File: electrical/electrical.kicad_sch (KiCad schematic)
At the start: 0 parts

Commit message: Added rotax
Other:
- sheet Rotax ports: added AIRCRAFT_AMPS_HI, AIRCRAFT_AMPS_LO, AIRCRAFT_GROUND, AIRCRAFT_POWER, ROTAX_CAN_GND, ROTAX_CAN_HI, ROTAX_CAN_LO; removed none
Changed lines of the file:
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@@
     (company "N915SN Angry Bird")
   )
-  (sheet (at 26.67 22.86) (size 20.32 25.4) (fields_autoplaced)
+  (sheet (at 19.05 19.05) (size 20.32 20.32) (fields_autoplaced)
     (stroke (width 0.1524) (type solid))
     (fill (color 0 0 0 0.0000))
-    (property "Sheetname" "Rotax" (at 26.67 22.1484 0)
+    (property "Sheetname" "Rotax" (at 19.05 18.3384 0)
       (effects (font (size 1.27 1.27)) (justify left bottom))
     )
-    (property "Sheetfile" "rotax.kicad_sch" (at 26.67 48.8446 0)
+    (property "Sheetfile" "rotax.kicad_sch" (at 19.05 39.9546 0)
       (effects (font (size 1.27 1.27)) (justify left top))
     )
+    (pin "AIRCRAFT_POWER" output (at 39.37 20.32 0)
+      (effects (font (size 1.27 1.27)) (justify right))
+    )
+    (pin "AIRCRAFT_GROUND" passive (at 39.37 22.86 0)
+      (effects (font (size 1.27 1.27)) (justify right))
+    )
+    (pin "AIRCRAFT_AMPS_HI" output (at 39.37 26.67 0)
+      (effects (font (size 1.27 1.27)) (justify right))
+    )
+    (pin "AIRCRAFT_AMPS_LO" output (at 39.37 29.21 0)
+      (effects (font (size 1.27 1.27)) (justify right))
+    )
+    (pin "ROTAX_CAN_LO" bidirectional (at 39.37 35.56 0)
+      (effects (font (size 1.27 1.27)) (justify right))
+    )
+    (pin "ROTAX_CAN_GND" passive (at 39.37 38.1 0)
+      (effects (font (size 1.27 1.27)) (justify right))
+    )
+    (pin "ROTAX_CAN_HI" bidirectional (at 39.37 33.02 0)
+      (effects (font (size 1.27 1.27)) (justify right))
+    )
     (instances

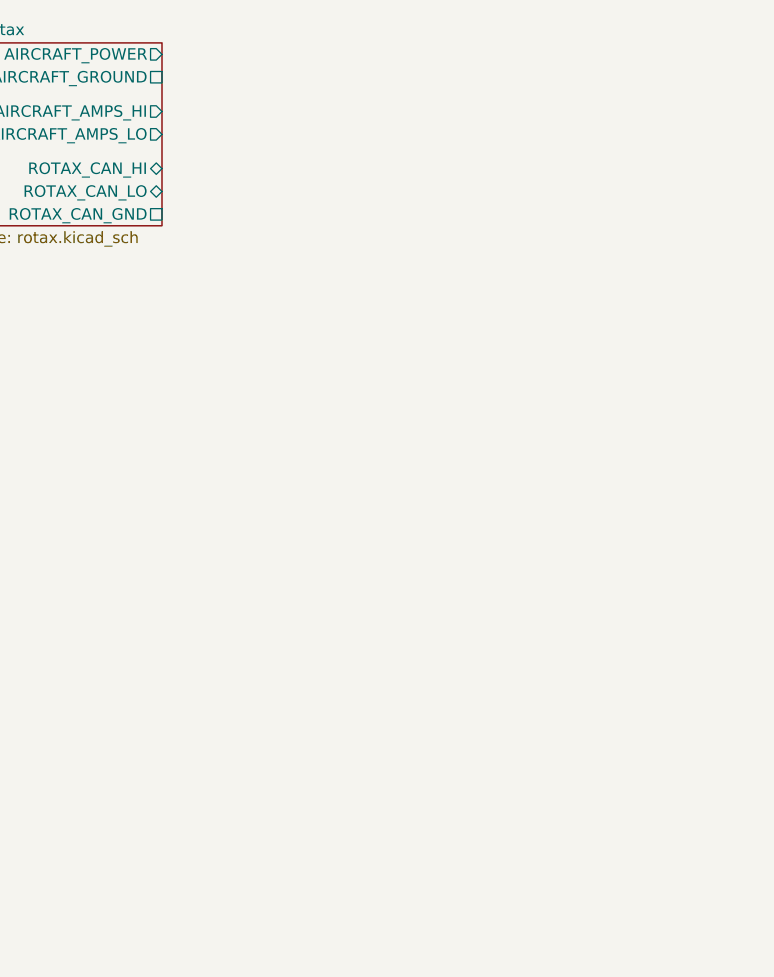
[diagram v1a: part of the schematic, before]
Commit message: Wired up power with GAD 27
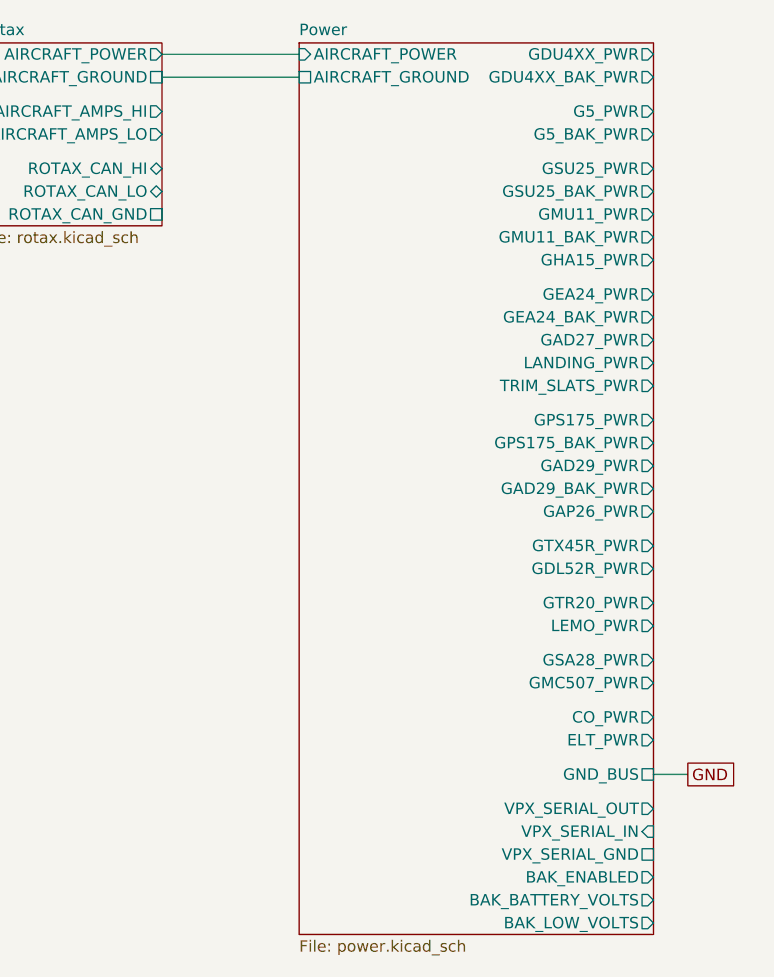
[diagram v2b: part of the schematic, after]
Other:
- added sheet Power (power.kicad_sch)
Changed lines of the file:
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@@
     (company "N915SN Angry Bird")
+  )
+  (wire (pts (xy 39.37 22.86) (xy 54.61 22.86))
+    (stroke (width 0) (type default))
+  )
+  (wire (pts (xy 93.98 100.33) (xy 97.79 100.33))
+    (stroke (width 0) (type default))
+  )
+  (wire (pts (xy 39.37 20.32) (xy 54.61 20.32))
+    (stroke (width 0) (type default))
+  )
+  (global_label "GND" (shape passive) (at 97.79 100.33 0) (fields_autoplaced)
+    (effects (font (size 1.27 1.27)) (justify left))
+    (property "Intersheetrefs" "${INTERSHEET_REFS}" (at 103.5344 100.33 0)
+      (effects (font (size 1.27 1.27)) (justify left) hide)
+    )
+  )
+  (sheet (at 54.61 19.05) (size 39.37 99.06) (fields_autoplaced)
+    (stroke (width 0.1524) (type solid))
+    (fill (color 0 0 0 0.0000))
+    (property "Sheetname" "Power" (at 54.61 18.3384 0)
+      (effects (font (size 1.27 1.27)) (justify left bottom))
+    )
+    (property "Sheetfile" "power.kicad_sch" (at 54.61 118.6946 0)
+      (effects (font (size 1.27 1.27)) (justify left top))
+    )
+    (pin "GND_BUS" passive (at 93.98 100.33 0)
+      (effects (font (size 1.27 1.27)) (justify right))
+    )
+    (pin "GDL52R_PWR" output (at 93.98 77.47 0)
+      (effects (font (size 1.27 1.27)) (justify right))
+    )
+    (pin "GTX45R_PWR" output (at 93.98 74.93 0)
+      (effects (font (size 1.27 1.27)) (justify right))
+    )
+    (pin "GAD29_PWR" output (at 93.98 66.04 0)
+      (effects (font (size 1.27 1.27)) (justify right))
+    )
+    (pin "GPS175_PWR" output (at 93.98 60.96 0)
+      (effects (font (size 1.27 1.27)) (justify right))
+    )
+    (pin "GMU11_PWR" output (at 93.98 38.1 0)
+      (effects (font (size 1.27 1.27)) (justify right))
+    )
+    (pin "GSU25_PWR" output (at 93.98 33.02 0)
+      (effects (font (size 1.27 1.27)) (justify right))
+    )
+    (pin "GHA15_PWR" output (at 93.98 43.18 0)
+      (effects (font (size 1.27 1.27)) (justify right))
+    )
+    (pin "CO_PWR" output (at 93.98 93.98 0)
+      (effects (font (size 1.27 1.27)) (justify right))
+    )
+    (pin "ELT_PWR" output (at 93.98 96.52 0)
+      (effects (font (size 1.27 1.27)) (justify right))
+    )
+    (pin "GEA24_BAK_PWR" output (at 93.98 49.53 0)
+      (effects (font (size 1.27 1.27)) (justify right))
+    )
+    (pin "GSU25_BAK_PWR" output (at 93.98 35.56 0)
+      (effects (font (size 1.27 1.27)) (justify right))
+    )
+    (pin "GDU4XX_BAK_PWR" output (at 93.98 22.86 0)
+      (effects (font (size 1.27 1.27)) (justify right))
+    )
+    (pin "GMU11_BAK_PWR" output (at 93.98 40.64 0)
+      (effects (font (size 1.27 1.27)) (justify right))
+    )
+    (pin "G5_BAK_PWR" output (at 93.98 29.21 0)
+      (effects (font (size 1.27 1.27)) (justify right))
+    )
+    (pin "GAD29_BAK_PWR" output (at 93.98 68.58 0)
+      (effects (font (size 1.27 1.27)) (justify right))
+    )
+    (pin "GPS175_BAK_PWR" output (at 93.98 63.5 0)
+      (effects (font (size 1.27 1.27)) (justify right))
+    )
+    (pin "AIRCRAFT_POWER" input (at 54.61 20.32 180)
+      (effects (font (size 1.27 1.27)) (justify left))
+    )
+    (pin "AIRCRAFT_GROUND" passive (at 54.61 22.86 180)
+      (effects (font (size 1.27 1.27)) (justify left))
+    )
+    (pin "GAP26_PWR" output (at 93.98 71.12 0)
+      (effects (font (size 1.27 1.27)) (justify right))
+    )
+    (pin "GDU4XX_PWR" output (at 93.98 20.32 0)
+      (effects (font (size 1.27 1.27)) (justify right))
+    )
+    (pin "GTR20_PWR" output (at 93.98 81.28 0)
+      (effects (font (size 1.27 1.27)) (justify right))
+    )
+    (pin "LEMO_PWR" output (at 93.98 83.82 0)
+      (effects (font (size 1.27 1.27)) (justify right))
+    )
+    (pin "G5_PWR" output (at 93.98 26.67 0)
+      (effects (font (size 1.27 1.27)) (justify right))
+    )
+    (pin "LANDING_PWR" output (at 93.98 54.61 0)
+      (effects (font (size 1.27 1.27)) (justify right))
+    )
+    (pin "TRIM_SLATS_PWR" output (at 93.98 57.15 0)
+      (effects (font (size 1.27 1.27)) (justify right))
+    )
+    (pin "BAK_BATTERY_VOLTS" output (at 93.98 114.3 0)
+      (effects (font (size 1.27 1.27)) (justify right))
+    )
+    (pin "BAK_ENABLED" output (at 93.98 111.76 0)
+      (effects (font (size 1.27 1.27)) (justify right))
+    )
+    (pin "BAK_LOW_VOLTS" output (at 93.98 116.84 0)
+      (effects (font (size 1.27 1.27)) (justify right))
+    )
+    (pin "GMC507_PWR" output (at 93.98 90.17 0)
+      (effects (font (size 1.27 1.27)) (justify right))
+    )
+    (pin "GSA28_PWR" output (at 93.98 87.63 0)
+      (effects (font (size 1.27 1.27)) (justify right))
+    )
+    (pin "VPX_SERIAL_IN" input (at 93.98 106.68 0)
+      (effects (font (size 1.27 1.27)) (justify right))
+    )
+    (pin "VPX_SERIAL_GND" passive (at 93.98 109.22 0)
+      (effects (font (size 1.27 1.27)) (justify right))
+    )
+    (pin "VPX_SERIAL_OUT" output (at 93.98 104.14 0)
+      (effects (font (size 1.27 1.27)) (justify right))
+    )
+    (pin "GEA24_PWR" output (at 93.98 46.99 0)
+      (effects (font (size 1.27 1.27)) (justify right))
+    )
+    (pin "GAD27_PWR" output (at 93.98 52.07 0)
+      (effects (font (size 1.27 1.27)) (justify right))
+    )
+    (instances
+      (project "electrical"
+        (path "/e8ec215a-dbe2-4eba-a577-e50a0a128049" (page "3"))
+      )
+    )
   )
   (sheet (at 19.05 19.05) (size 20.32 20.32) (fields_autoplaced)
